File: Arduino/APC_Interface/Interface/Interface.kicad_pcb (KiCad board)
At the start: 2 copper layers, 62.2 x 35.6 mm, 10 parts, among them J1 UPS_Interface, Q1 PN100, Q2 PN100, U1 LEOSTICK_SHIELD

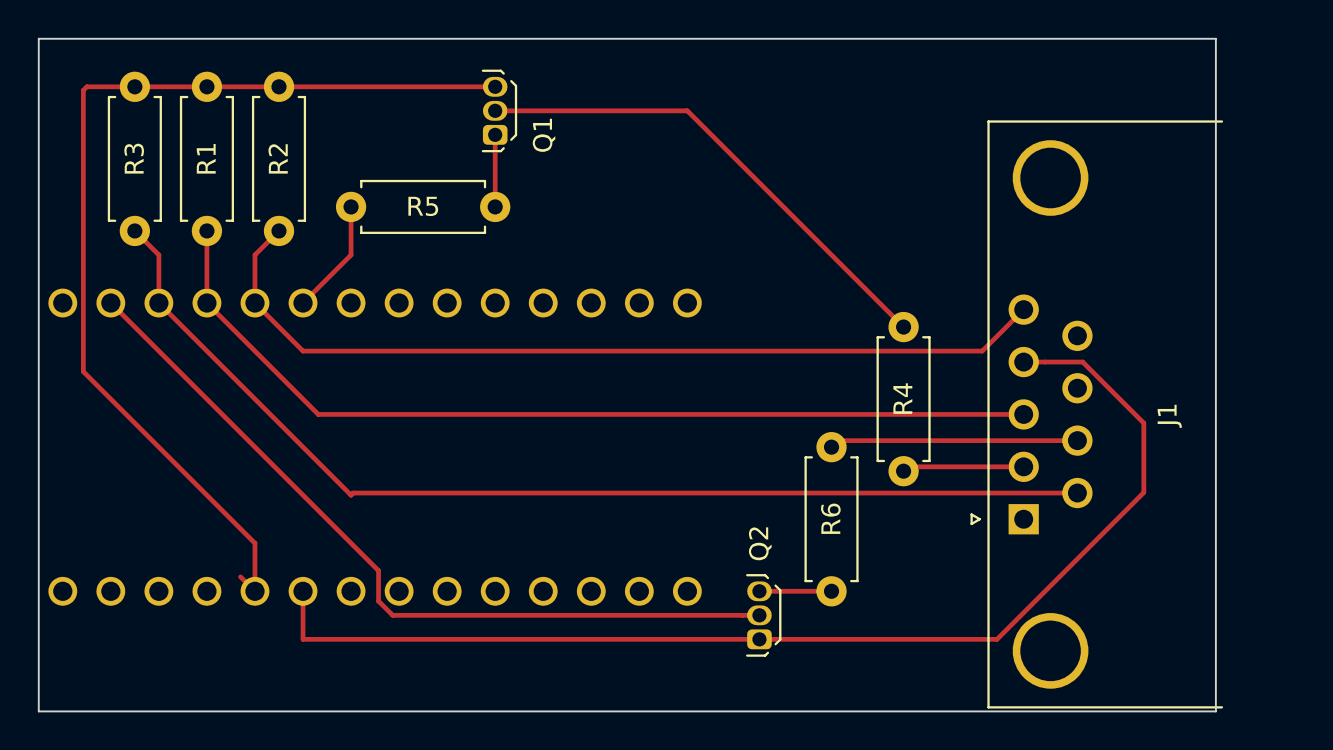
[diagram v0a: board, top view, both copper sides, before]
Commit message: Updated schematic & layout, floating ground
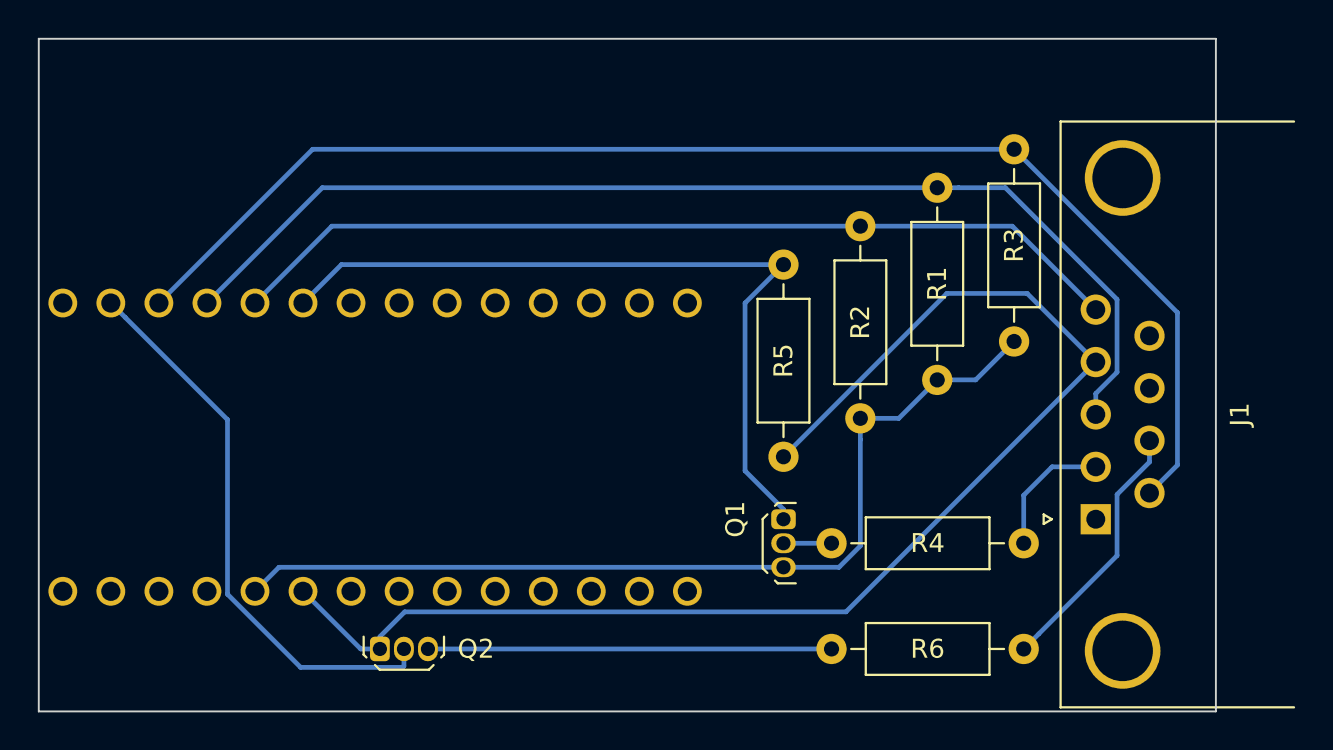
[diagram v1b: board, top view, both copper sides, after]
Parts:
- R1, R2, R3, R4, R5, R6: footprint Resistor_THT:R_Axial_DIN0207_L6.3mm_D2.5mm_P7.62mm_Horizontal -> Resistor_THT:R_Axial_DIN0207_L6.3mm_D2.5mm_P10.16mm_Horizontal
- moved R3 48.4 mm to (79.5, 32.5), turned to 90 degrees
- moved R1 41.6 mm to (75.4, 34.5), turned to 90 degrees
- moved R2 35.4 mm to (71.4, 36.6), turned to 90 degrees
- moved Q1 25.4 mm to (67.3, 41.9), turned to 270 degrees
- moved R5 20.2 mm to (67.3, 38.6), turned to 90 degrees
- moved Q2 20.1 mm to (46.0, 48.8), turned to 0 degrees
- moved R4 7.41 mm to (80.0, 43.2), turned to 180 degrees
- moved J1 3.81 mm to (83.8, 41.9)
- moved R6 3.05 mm to (69.8, 48.8), turned to 0 degrees
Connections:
- R5 pad 1: Net-(Q1-Pad1) -> GND
- R5 pad 2: Net-(R5-Pad2) -> Net-(Q1-Pad1)
- U1 pad 8: Net-(R5-Pad2) -> Net-(Q1-Pad1)
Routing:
- net Net-(Q1-Pad1): track 3.81 -> 41.4 mm
- net Net-(Q1-Pad2): track 26.3 -> 2.54 mm
- net Net-(Q2-Pad3): track 3.81 -> 21.3 mm
- net Net-(J1-Pad6): track 57.2 -> 70.9 mm
- net Net-(Q2-Pad2): track 42.1 -> 29.8 mm
- net Net-(J1-Pad3): track 49.4 -> 59.6 mm
- net GND: track 61.6 -> 71.4 mm
- net Net-(R5-Pad2): track 6.13 -> 0.00 mm
- net Net-(Q1-Pad3): track 53.2 -> 49.6 mm
- net Net-(J1-Pad5): track 46.9 -> 48.0 mm
- net Net-(J1-Pad2): track 6.45 -> 7.20 mm
- net Net-(J1-Pad7): track 13.1 -> 13.8 mm
